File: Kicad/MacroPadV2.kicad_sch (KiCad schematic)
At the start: 56 parts, among them J1 3PinJump, J2 3PinJump, J3 GCT-USB4085, J4 3PinJump, J5 4PinJump, J6 4PinJump, K1 KSW, K10 KSW, K11 KSW, K12 KSW, K2 KSW, K3 KSW, K4 KSW, K5 KSW, K6 KSW, K7 KSW, K8 KSW, K9 KSW, SW1 SWITCH_TACTILE_SPST-NO_0.05A_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, SW2 SWITCH_TACTILE_SPST-NO_0.05A_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, SW3 RotaryEncoder_Switch, U1 STM32F103C8T6TR, U2 AP2114HA-3.3TRG1, X1 TSX-3225_16.0000MF18X-AC6

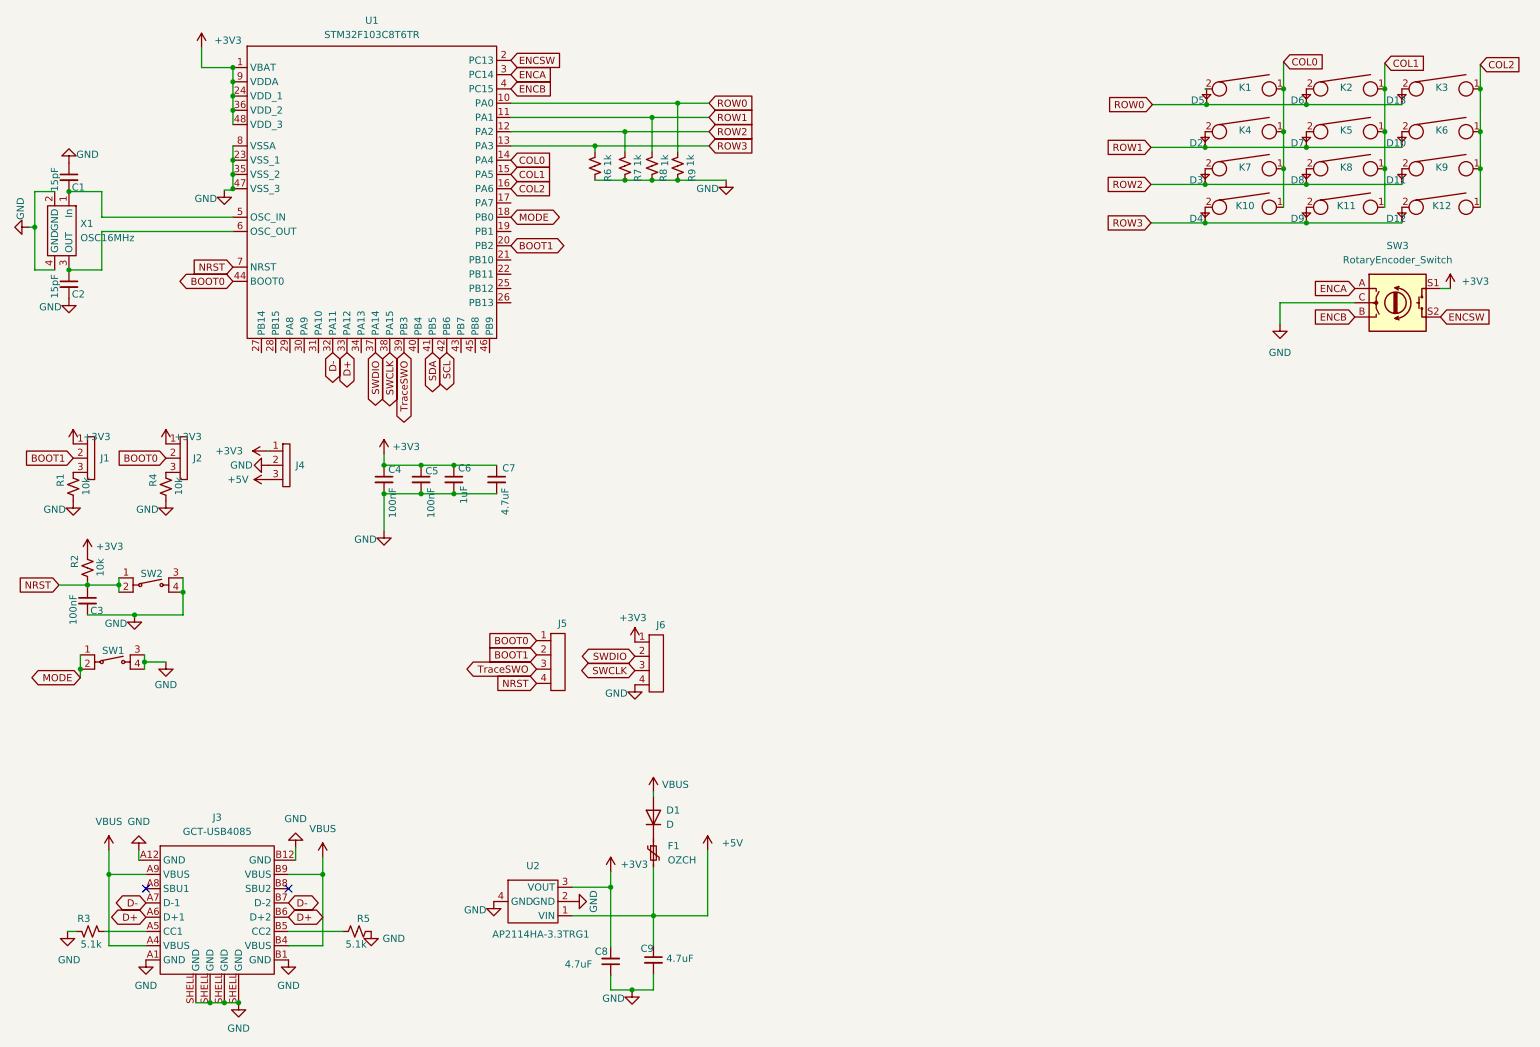
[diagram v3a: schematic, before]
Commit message: Fully Finished MacroPad V2 Schematic and Layout with stm32. Ordered and waiting for board to come in. 	-If there are no issues running the board, this should be the last commit for Kicad files. All proceeding commits should be code 	-Added gitignore with the kicad backup folder to keep backups from being added to git
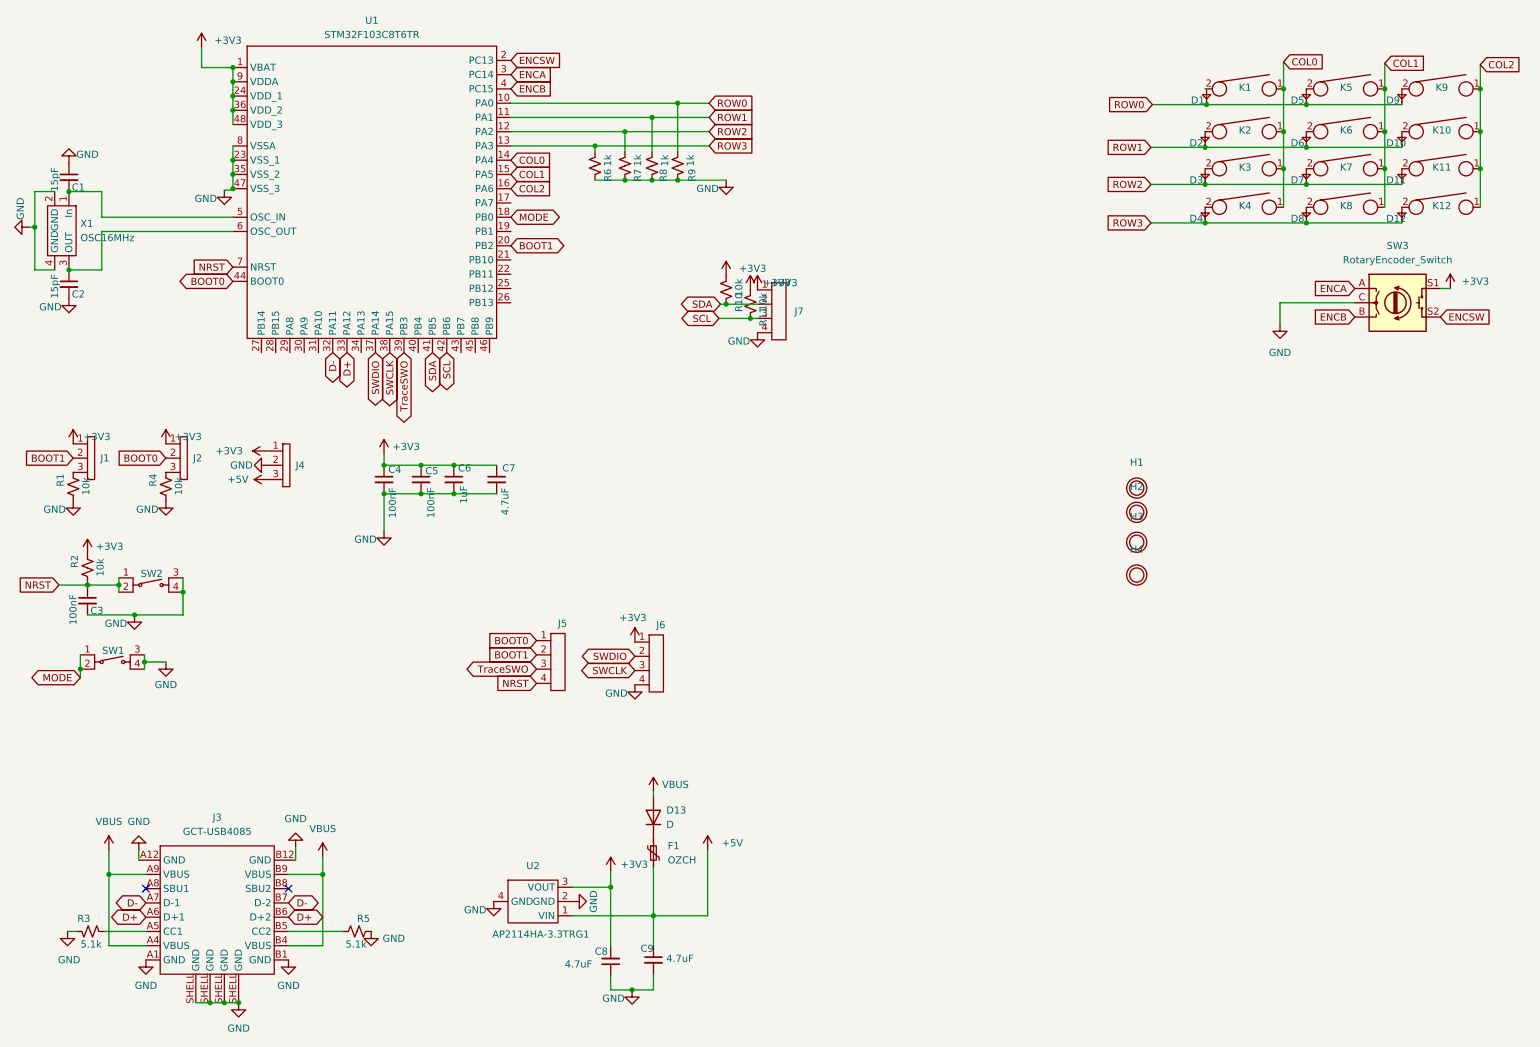
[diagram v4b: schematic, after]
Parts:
- added H1, H2, H3, H4: M3Hole, mpadfps:M3Hole, symbol macropad_parts:M3Hole
- added J7: 4PinJump, Connector_PinHeader_2.54mm:PinHeader_1x04_P2.54mm_Vertical, symbol macropad_parts:4PinJump
- added R10, R11: 10k, Resistor_SMD:R_0805_2012Metric_Pad1.20x1.40mm_HandSolder, symbol Device:R_Small_US
- C1, C2: DigikeyPN (none) -> 311-1101-2-ND
- C3, C4, C5: DigikeyPN (none) -> 3372-MT05B104M500BDTR-ND
- C6: DigikeyPN (none) -> 1276-1003-2-ND
- C7, C8, C9: DigikeyPN (none) -> 1276-1244-2-ND
- D1: renamed from D5; value 1N4148WX-TP -> TS4148 RBG; DigikeyPN (none) -> 1801-TS4148RBGTR-ND
- D10, D11, D12, D2, D3, D4: value 1N4148WX-TP -> TS4148 RBG; DigikeyPN (none) -> 1801-TS4148RBGTR-ND
- D13: renamed from D1; DigikeyPN (none) -> 1801-TS4148RBGTR-ND
- D5: renamed from D6; value 1N4148WX-TP -> TS4148 RBG; DigikeyPN (none) -> 1801-TS4148RBGTR-ND
- D6: renamed from D7; value 1N4148WX-TP -> TS4148 RBG; DigikeyPN (none) -> 1801-TS4148RBGTR-ND
- D7: renamed from D8; value 1N4148WX-TP -> TS4148 RBG; DigikeyPN (none) -> 1801-TS4148RBGTR-ND
- D8: renamed from D9; value 1N4148WX-TP -> TS4148 RBG; DigikeyPN (none) -> 1801-TS4148RBGTR-ND
- D9: renamed from D13; value 1N4148WX-TP -> TS4148 RBG; DigikeyPN (none) -> 1801-TS4148RBGTR-ND
- F1: DigikeyPN (none) -> 507-1792-2-ND
- K1, K12: DigikeyPN (none) -> CH197-ND
- K10: renamed from K6; DigikeyPN (none) -> CH197-ND
- K11: renamed from K9; DigikeyPN (none) -> CH197-ND
- K2: renamed from K4; DigikeyPN (none) -> CH197-ND
- K3: renamed from K7; DigikeyPN (none) -> CH197-ND
- K4: renamed from K10; DigikeyPN (none) -> CH197-ND
- K5: renamed from K2; DigikeyPN (none) -> CH197-ND
- K6: renamed from K5; DigikeyPN (none) -> CH197-ND
- K7: renamed from K8; DigikeyPN (none) -> CH197-ND
- K8: renamed from K11; DigikeyPN (none) -> CH197-ND
- K9: renamed from K3; DigikeyPN (none) -> CH197-ND
- R1, R2, R4: DigikeyPN (none) -> RMCF0805JT10K0TR-ND
- R3, R5: DigikeyPN (none) -> RMCF0805JT5K10TR-ND
- R6, R7, R8, R9: DigikeyPN (none) -> RMCF0805FT1K00
- SW1, SW2: DigikeyPN (none) -> CKN9085TR-ND
- SW3: DigikeyPN (none) -> 118-PEC11H-4220F-S0024-ND
- U1: footprint mpadfps:LQFP48 -> macrofp:LQFP48; DigikeyPN (none) -> 497-17666-2-ND
- U2: DigikeyPN (none) -> AP2114HA-3.3TRG1DITR-ND
- X1: DigikeyPN (none) -> SER4372TR-ND
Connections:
- net +3V3: now also J7.1, R10.2, R11.2
- net GND: now also J7.4
- net SCL: now also J7.3, R11.1
- net SDA: now also J7.2, R10.1

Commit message: Removed some backups and push for swap to desktop
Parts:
- removed J5, J6: 4PinJump, Connector_PinHeader_2.54mm:PinHeader_1x04_P2.54mm_Vertical, symbol macropad_parts:4PinJump
- added J5: 7PinHeader, Connector_PinHeader_2.54mm:PinHeader_1x07_P2.54mm_Vertical, symbol macropad_parts:7PinHeader
- U1: footprint macrofp:LQFP48 -> mpadfps:LQFP48
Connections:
- net +3V3: now also J5.1
- net D+: no longer J3.B6 (D+2)
- net D-: no longer J3.B7 (D-2)
- net GND: now also J5.7; no longer J3.SHELL (GND)
- net SWDIO/JTMS: now reaches U1.34 (PA13)
- net SWDIO/JTMS: now also J5.2
- net JTNRST: now reaches U1.40 (PB4)
- net JTNRST: now also J5.6
- net SWCLK renamed JTDI
- net JTDI: now also J5.4
- net SWDIO renamed SWCLK/JTCK
- net SWCLK/JTCK: now also J5.3
- net TraceSWO renamed JTDO
- net JTDO: now also J5.5
- no-connect marks 2 -> 6
